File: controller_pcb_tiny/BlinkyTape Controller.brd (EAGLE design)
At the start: 32 x 10 mm, 27 parts, among them CON1 USB_MICROSMT+THRUHULE, Q1 16MHz, U1 MK20D--VFM5, U2 SPI-FLASHSO-8, U3 BRM-2508SMD, U4 74LVC1G17DCK, U6 TPD4S012

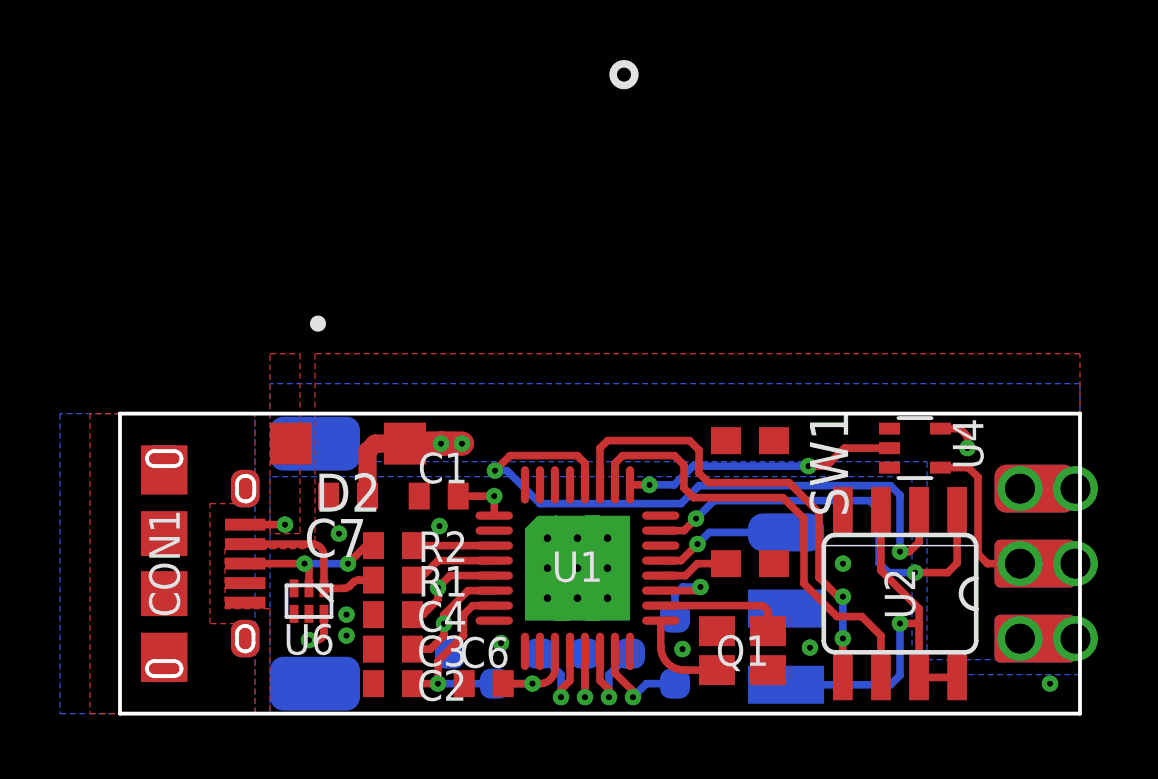
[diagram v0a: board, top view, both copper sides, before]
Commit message: Rework board to be 29mm, use 0603 package for main cap, add bottom side pad for VUSB, improve +5V routing
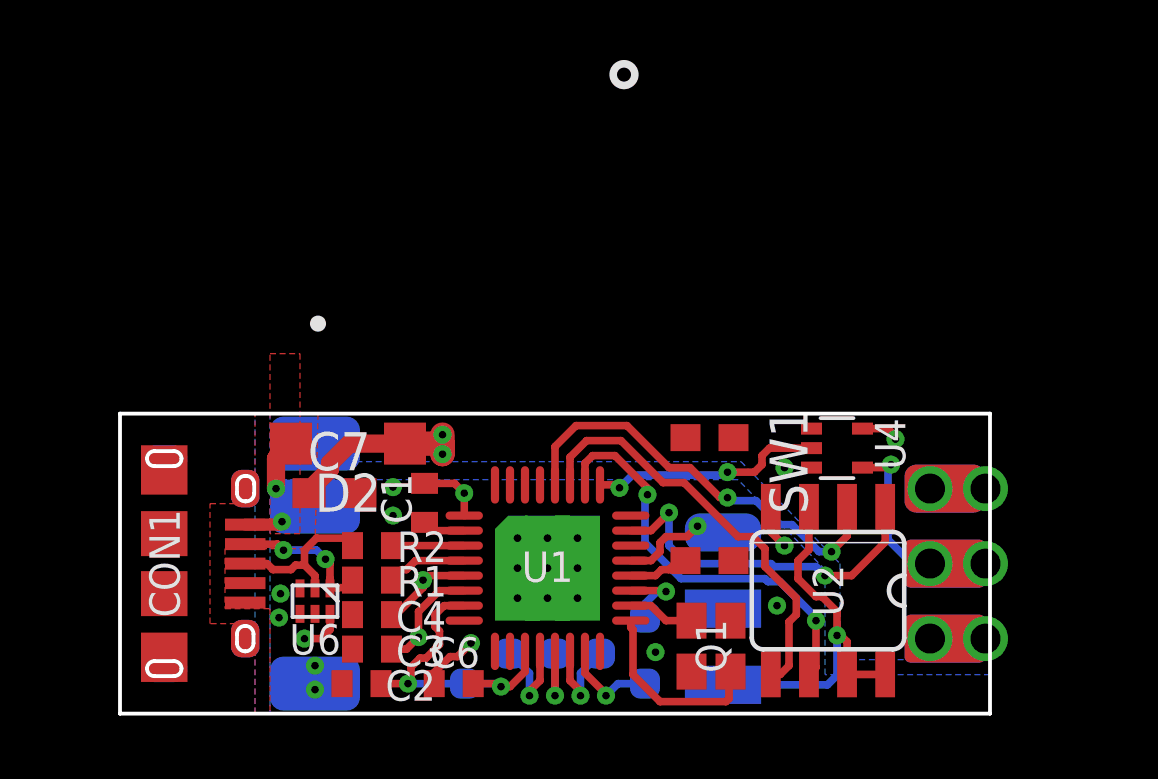
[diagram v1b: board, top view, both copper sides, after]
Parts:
- removed U$5: POGO_PINSMD, blinkinlabs:POGO_PIN_SMD
- added RECT_PAD1: TEST_PAD_SMTRECT_PAD, blinkinlabs:TEST_PAD_SMT
- C7: device adafruit:C0402 -> adafruit:C0603
- moved U$1 3.00 mm to (27.5, 5.00)
- moved U4 2.60 mm to (23.9, 8.85)
- moved U2 2.40 mm to (23.6, 4.10)
- moved U3 2.10 mm to (20.1, 3.50)
- moved SW1 1.35 mm to (19.6, 7.20)
- moved Q1 1.06 mm to (19.7, 2.25), turned to 270 degrees
- moved C2 1.05 mm to (8.05, 1.00)
- moved C6 1.00 mm to (11.1, 1.00)
- moved U$2 1.00 mm to (11.5, 1.00)
- moved U$3 1.00 mm to (13.0, 2.00)
- moved U$4 1.00 mm to (16.0, 2.00)
- moved U$6 1.00 mm to (14.5, 2.00)
- moved U$7 1.00 mm to (17.5, 1.00)
- moved U$8 1.00 mm to (17.5, 3.20)
- moved U1 1.00 mm to (14.2, 4.85)
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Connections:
- net GND: no longer U$5.P$1
- net VUSB: now also RECT_PAD1.P$1
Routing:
- net FLASH_MISO: track 22.1 -> 14.3 mm
- net GND: track 0.00 -> 4.93 mm, vias 9 -> 11
- net VUSB: track 2.55 -> 6.02 mm, vias 2 -> 3
- net N$2: track 3.07 -> 6.37 mm
- net FLASH_CS: track 14.2 -> 11.9 mm
- net N$1: track 4.28 -> 2.23 mm
- net FLASH_MOSI: track 16.0 -> 14.3 mm, vias 2 -> 0
- net FLASH_SCK: track 15.3 -> 13.9 mm, vias 0 -> 2
- net DATA_OUT: track 9.16 -> 7.82 mm
- net +5V: track 10.3 -> 11.3 mm
- net IR_REC: track 4.56 -> 3.81 mm
- net RESET: track 3.10 -> 2.54 mm
- net LED_DATA: track 7.33 -> 7.11 mm, vias 0 -> 1
- net N$7: track 5.61 -> 5.50 mm, vias 0 -> 2
- net N$10: track 5.41 -> 5.47 mm, vias 2 -> 0
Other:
- board size 32 x 10 mm -> 29 x 10 mm
- board text removed: "CON3"

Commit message: RevA tiny controller
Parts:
- added U$5, U$9: POGO_PINSMD, blinkinlabs:POGO_PIN_SMD
- U$1: value WS2812B_CONNECTORSTANDARD -> WS2812B_CONNECTOR; device blinkinlabs:WS2812B_CONNECTOR -> blinkinlabs:WS2812B_CONNECTOR_COMBINED
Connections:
- net +5V: now also U$1.5V2, U$1.5V_3
- net GND: now also U$1.GND_3, U$1.GND_4
- net PD5: now also U$5.P$1
- net PD6: now also U$9.P$1
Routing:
- net PD6: track 0.00 -> 2.11 mm
- net PD5: track 0.00 -> 1.64 mm
